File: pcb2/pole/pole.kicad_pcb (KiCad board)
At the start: 2 copper layers, 17 x 49 mm, 23 parts, among them IC1 LMx93, IC2 STM32F0xxKxUx, P1 POWER_IN, P2 BUS_IN, P3 BUS_OUT, P4 SWD_TC, P5 LEDs, Q1 MTM232270LBF, Q2 MTM232270LBF, Q3 MTM232270LBF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

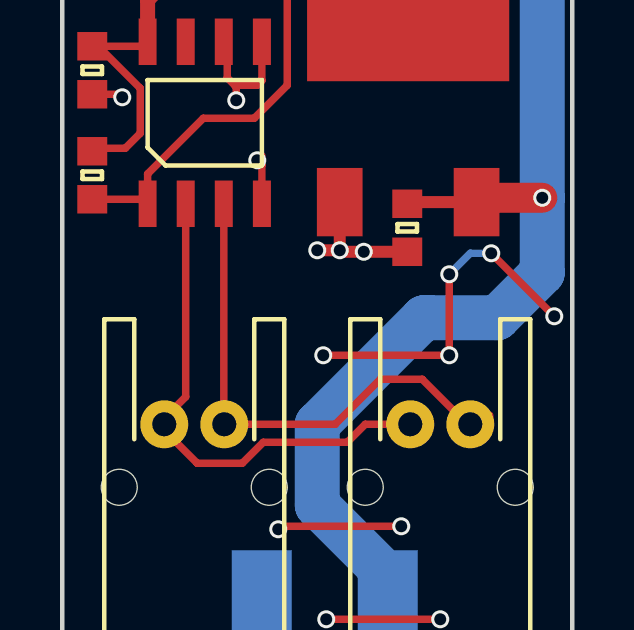
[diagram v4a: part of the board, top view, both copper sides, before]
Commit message: Added comparator receiver hysteresis
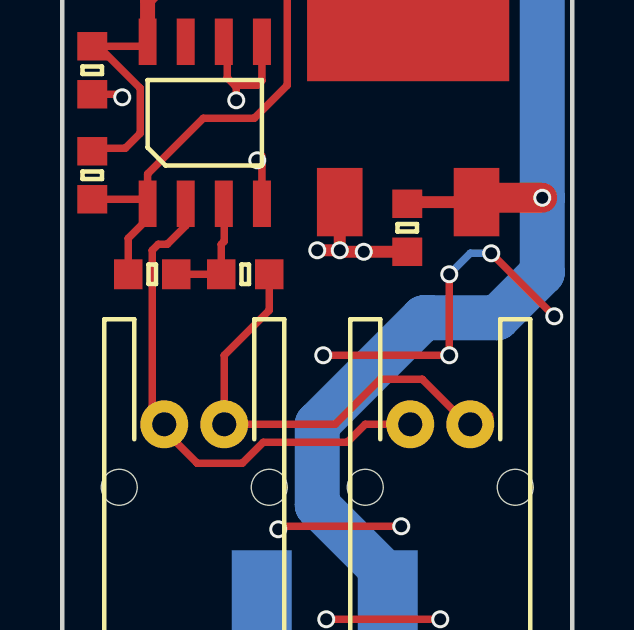
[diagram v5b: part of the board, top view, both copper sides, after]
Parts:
- added R2: 10k, agg:0603, F.Cu at (122.1, 101.3)
- added R3: 1M, agg:0603, F.Cu at (119.0, 101.3)
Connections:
- IC1 pad 3: /BUS_B -> Net-(IC1-Pad3)
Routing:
- net Net-(IC1-Pad3): track 0.00 -> 3.99 mm
- net /BUS: track 26.3 -> 29.0 mm
- net /BUS_B: track 17.5 -> 15.7 mm
- net /BUS_A: track 17.1 -> 17.8 mm
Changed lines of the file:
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@@
 (kicad_pcb (version 4) (host pcbnew 4.0.2-4+6225~38~ubuntu15.10.1-stable)
   (general
-    (links 59)
+    (links 62)
     (no_connects 0)
-    (area 114.894048 65.810714 134.355 127.725001)
+    (area 115.924999 65.924999 133.075001 115.075001)
     (thickness 1.6)
     (drawings 4)
-    (tracks 243)
+    (tracks 260)
     (zones 0)
-    (modules 23)
-    (nets 18)
+    (modules 25)
+    (nets 19)
   )
   (page A4)
@@
   (net 16 /LED_B)
   (net 17 "Net-(IC2-Pad4)")
+  (net 18 "Net-(IC1-Pad3)")
   (net_class Default "This is the default net class."
     (clearance 0.15)
@@
     (add_net /SWDIO)
     (add_net GND)
+    (add_net "Net-(IC1-Pad3)")
     (add_net "Net-(IC2-Pad4)")
     (add_net "Net-(Q4-Pad3)")
@@
       (net 5 /BUS_A))
     (pad 3 smd rect (at -2.7 0.635 90) (size 1.55 0.6) (layers F.Cu F.Paste F.Mask)
-      (net 6 /BUS_B))
+      (net 18 "Net-(IC1-Pad3)"))
     (pad 4 smd rect (at -2.7 1.905 90) (size 1.55 0.6) (layers F.Cu F.Paste F.Mask)
       (net 1 GND))
@@
     (pad 1 smd circle (at 0 0) (size 1 1) (layers F.Cu F.Mask)
       (net 17 "Net-(IC2-Pad4)"))
+  )
+  (module agg:0603 (layer F.Cu)
+    (at 122.1 101.3)
+    (fp_text reference R2 (at -2.225 0 90) (layer F.Fab) hide
+      (effects (font (size 1 1) (thickness 0.15)))
+    )
+    (fp_text value 10k (at 2.225 0 90) (layer F.Fab) hide
+      (effects (font (size 1 1) (thickness 0.15)))
+    )
+    (fp_line (start -0.8 -0.4) (end 0.8 -0.4) (layer F.Fab) (width 0.01))
+    (fp_line (start 0.8 -0.4) (end 0.8 0.4) (layer F.Fab) (width 0.01))
+    (fp_line (start 0.8 0.4) (end -0.8 0.4) (layer F.Fab) (width 0.01))
+    (fp_line (start -0.8 0.4) (end -0.8 -0.4) (layer F.Fab) (width 0.01))
+    (fp_line (start -0.45 -0.4) (end -0.45 0.4) (layer F.Fab) (width 0.01))
+    (fp_line (start 0.45 -0.4) (end 0.45 0.4) (layer F.Fab) (width 0.01))
+    (fp_line (start -0.125 -0.325) (end 0.125 -0.325) (layer F.SilkS) (width 0.15))
+    (fp_line (start 0.125 -0.325) (end 0.125 0.325) (layer F.SilkS) (width 0.15))
+    (fp_line (start 0.125 0.325) (end -0.125 0.325) (layer F.SilkS) (width 0.15))
+    (fp_line (start -0.125 0.325) (end -0.125 -0.325) (layer F.SilkS) (width 0.15))
+    (fp_line (start -1.55 -0.75) (end 1.55 -0.75) (layer F.CrtYd) (width 0.01))
+    (fp_line (start 1.55 -0.75) (end 1.55 0.75) (layer F.CrtYd) (width 0.01))
+    (fp_line (start 1.55 0.75) (end -1.55 0.75) (layer F.CrtYd) (width 0.01))
+    (fp_line (start -1.55 0.75) (end -1.55 -0.75) (layer F.CrtYd) (width 0.01))
+    (pad 1 smd rect (at -0.8 0) (size 0.95 1) (layers F.Cu F.Paste F.Mask)
+      (net 18 "Net-(IC1-Pad3)"))
+    (pad 2 smd rect (at 0.8 0) (size 0.95 1) (layers F.Cu F.Paste F.Mask)
+      (net 6 /BUS_B))
+  )
+  (module agg:0603 (layer F.Cu)
+    (at 119 101.3)
+    (fp_text reference R3 (at -2.225 0 90) (layer F.Fab) hide
+      (effects (font (size 1 1) (thickness 0.15)))
+    )
+    (fp_text value 1M (at 2.225 0 90) (layer F.Fab) hide
+      (effects (font (size 1 1) (thickness 0.15)))
+    )
+    (fp_line (start -0.8 -0.4) (end 0.8 -0.4) (layer F.Fab) (width 0.01))
+    (fp_line (start 0.8 -0.4) (end 0.8 0.4) (layer F.Fab) (width 0.01))
+    (fp_line (start 0.8 0.4) (end -0.8 0.4) (layer F.Fab) (width 0.01))
+    (fp_line (start -0.8 0.4) (end -0.8 -0.4) (layer F.Fab) (width 0.01))
+    (fp_line (start -0.45 -0.4) (end -0.45 0.4) (layer F.Fab) (width 0.01))
+    (fp_line (start 0.45 -0.4) (end 0.45 0.4) (layer F.Fab) (width 0.01))
+    (fp_line (start -0.125 -0.325) (end 0.125 -0.325) (layer F.SilkS) (width 0.15))
+    (fp_line (start 0.125 -0.325) (end 0.125 0.325) (layer F.SilkS) (width 0.15))
+    (fp_line (start 0.125 0.325) (end -0.125 0.325) (layer F.SilkS) (width 0.15))
+    (fp_line (start -0.125 0.325) (end -0.125 -0.325) (layer F.SilkS) (width 0.15))
+    (fp_line (start -1.55 -0.75) (end 1.55 -0.75) (layer F.CrtYd) (width 0.01))
+    (fp_line (start 1.55 -0.75) (end 1.55 0.75) (layer F.CrtYd) (width 0.01))
+    (fp_line (start 1.55 0.75) (end -1.55 0.75) (layer F.CrtYd) (width 0.01))
+    (fp_line (start -1.55 0.75) (end -1.55 -0.75) (layer F.CrtYd) (width 0.01))
+    (pad 1 smd rect (at -0.8 0) (size 0.95 1) (layers F.Cu F.Paste F.Mask)
+      (net 4 /BUS))
+    (pad 2 smd rect (at 0.8 0) (size 0.95 1) (layers F.Cu F.Paste F.Mask)
+      (net 18 "Net-(IC1-Pad3)"))
   )
   (gr_line (start 133 115) (end 116 115) (angle 90) (layer Edge.Cuts) (width 0.15))
@@
   (segment (start 130.25 68) (end 128.33 68) (width 1.5) (layer B.Cu) (net 3))
   (segment (start 130.475 98.95) (end 130.53 98.895) (width 0.25) (layer F.Cu) (net 3))
+  (segment (start 118.2 101.3) (end 118.2 100.1) (width 0.25) (layer F.Cu) (net 4))
+  (segment (start 118.2 100.1) (end 118.9 99.4) (width 0.25) (layer F.Cu) (net 4))
+  (segment (start 118.9 99.4) (end 118.9 99) (width 0.25) (layer F.Cu) (net 4))
+  (segment (start 118.9 99) (end 118.845 98.95) (width 0.25) (layer F.Cu) (net 4))
   (segment (start 118.845 98.95) (end 118.845 97.955) (width 0.25) (layer F.Cu) (net 4))
   (segment (start 120.5 83.2) (end 120.5 82.1) (width 0.25) (layer F.Cu) (net 4))
@@
   (segment (start 118.695 98.8) (end 118.845 98.95) (width 0.25) (layer F.Cu) (net 4))
   (segment (start 116.85 98.95) (end 116.75 99.05) (width 0.25) (layer F.Cu) (net 4))
+  (segment (start 120.115 98.95) (end 120.115 99.685) (width 0.25) (layer F.Cu) (net 5))
+  (segment (start 120.115 99.685) (end 119.5 100.3) (width 0.25) (layer F.Cu) (net 5))
+  (segment (start 119.5 100.3) (end 119.2 100.3) (width 0.25) (layer F.Cu) (net 5))
+  (segment (start 119.2 100.3) (end 119 100.5) (width 0.25) (layer F.Cu) (net 5))
+  (segment (start 119 100.5) (end 119 105.7) (width 0.25) (layer F.Cu) (net 5))
+  (segment (start 119 105.7) (end 119.4 106.1) (width 0.25) (layer F.Cu) (net 5))
+  (segment (start 119.4 106.1) (end 119.4 106.3) (width 0.25) (layer F.Cu) (net 5))
   (segment (start 127.6 106.3) (end 126.1 106.3) (width 0.25) (layer F.Cu) (net 5))
   (segment (start 120.5 107.6) (end 119.4 106.5) (width 0.25) (layer F.Cu) (net 5))
@@
   (segment (start 119.4 106.5) (end 119.4 106.3) (width 0.25) (layer F.Cu) (net 5))
   (segment (start 127.7 106.3) (end 127.6 106.3) (width 0.25) (layer F.Cu) (net 5))
-  (segment (start 120.115 98.95) (end 120.115 105.385) (width 0.25) (layer F.Cu) (net 5))
-  (segment (start 120.115 105.385) (end 119.4 106.1) (width 0.25) (layer F.Cu) (net 5))
   (segment (start 119.4 106.1) (end 119.4 106.3) (width 0.25) (layer F.Cu) (net 5))
+  (segment (start 121.4 106.3) (end 121.4 104) (width 0.25) (layer F.Cu) (net 6))
+  (segment (start 122.9 102.5) (end 122.9 101.3) (width 0.25) (layer F.Cu) (net 6))
+  (segment (start 121.4 104) (end 122.9 102.5) (width 0.25) (layer F.Cu) (net 6))
   (segment (start 121.4 106.3) (end 125.1 106.3) (width 0.25) (layer F.Cu) (net 6))
   (segment (start 128 104.8) (end 129.5 106.3) (width 0.25) (layer F.Cu) (net 6))
@@
   (segment (start 125.1 106.3) (end 126.6 104.8) (width 0.25) (layer F.Cu) (net 6))
   (segment (start 129.5 106.3) (end 129.6 106.3) (width 0.25) (layer F.Cu) (net 6))
-  (segment (start 121.385 98.95) (end 121.385 106.415) (width 0.25) (layer F.Cu) (net 6))
   (segment (start 121.385 106.415) (end 121.3 106.5) (width 0.25) (layer F.Cu) (net 6))
   (segment (start 121.3 106.5) (end 121.4 106.3) (width 0.25) (layer F.Cu) (net 6))
@@
   (segment (start 119.9 79.5) (end 119 79.5) (width 0.25) (layer F.Cu) (net 17))
   (segment (start 119 79.5) (end 118.6 79.1) (width 0.25) (layer F.Cu) (net 17))
+  (segment (start 119.8 101.3) (end 121.1 101.3) (width 0.25) (layer F.Cu) (net 18))
+  (segment (start 121.1 101.3) (end 121.3 101.3) (width 0.25) (layer F.Cu) (net 18))
+  (segment (start 121.3 101.3) (end 121.3 100.3) (width 0.25) (layer F.Cu) (net 18))
+  (segment (start 121.4 100.2) (end 121.4 98.9) (width 0.25) (layer F.Cu) (net 18))
+  (segment (start 121.3 100.3) (end 121.4 100.2) (width 0.25) (layer F.Cu) (net 18))
+  (segment (start 121.4 98.9) (end 121.385 98.95) (width 0.25) (layer F.Cu) (net 18))
   (zone (net 1) (net_name GND) (layer B.Cu) (hatch edge 0.508)
     (connect_pads (clearance 0.25))

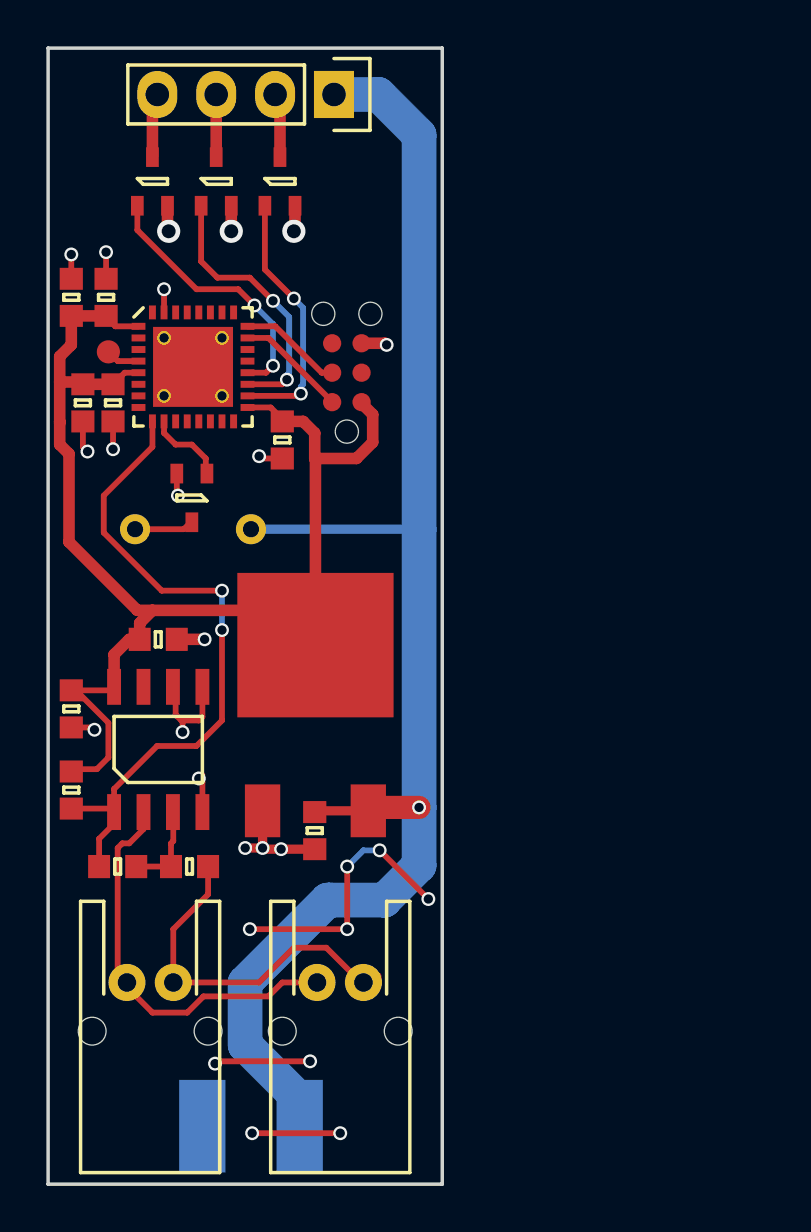
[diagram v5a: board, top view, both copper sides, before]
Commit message: re-layout and reroute of pole pcb
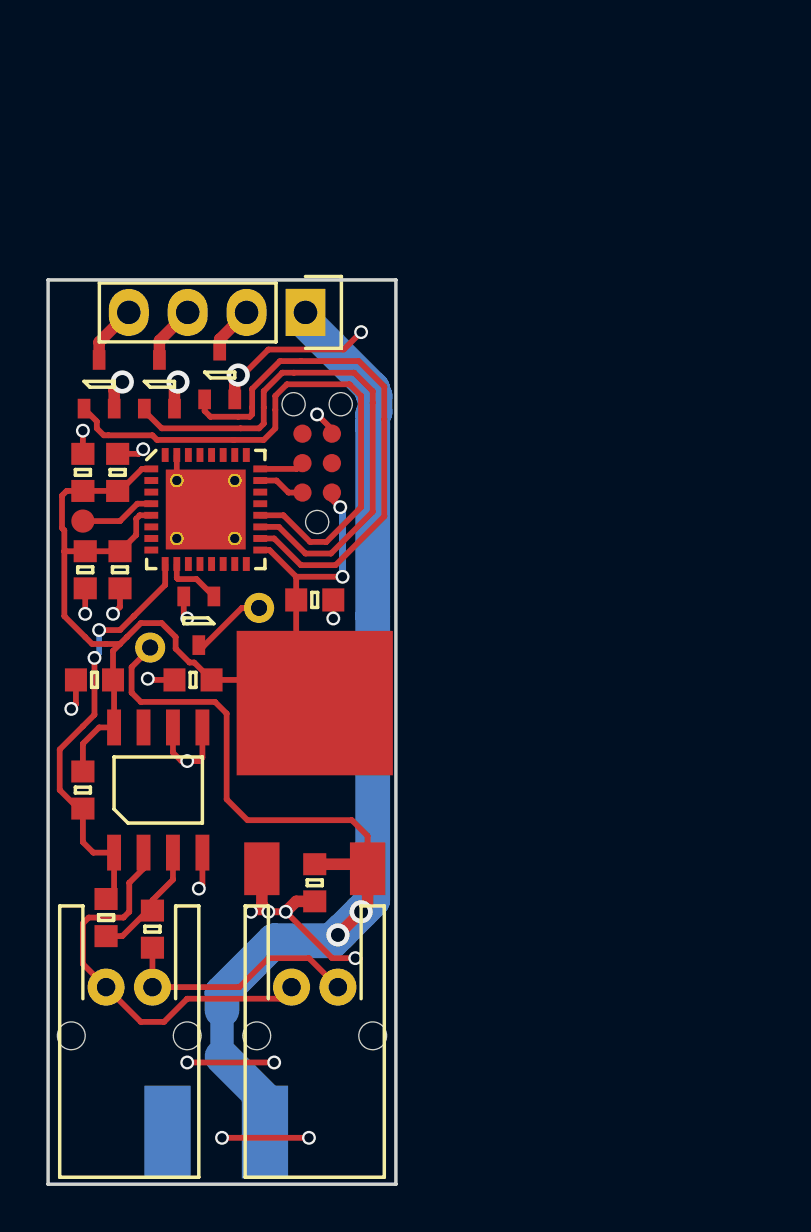
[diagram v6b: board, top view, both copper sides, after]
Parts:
- moved P5 9.48 mm to (127.1, 77.4)
- moved Q2 9.09 mm to (120.8, 80.5)
- moved Q3 9.05 mm to (118.2, 80.5)
- moved Q1 8.75 mm to (123.4, 80.1)
- moved C2 7.57 mm to (117.5, 84.3)
- moved C3 7.57 mm to (119.0, 84.3)
- moved TP1 7.38 mm to (117.5, 86.4)
- moved C4 7.21 mm to (119.1, 88.5)
- moved C8 7.20 mm to (117.6, 88.5)
- moved C5 7.04 mm to (127.5, 89.8), turned to 0 degrees
- moved IC2 6.17 mm to (122.8, 85.9)
- moved Q4 5.31 mm to (122.5, 90.7)
- moved SP1 4.28 mm to (122.8, 91.0), turned to 20 degrees
- moved P4 4.10 mm to (127.6, 83.9)
- moved R2 3.14 mm to (120.5, 104.0), turned to 270 degrees
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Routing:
- net /LED_B: track 11.6 -> 25.0 mm, vias 2 -> 0
- net (no net): track 19.5 -> 7.50 mm, vias 9 -> 4
- net /LED_G: track 11.7 -> 23.7 mm, vias 2 -> 0
- net /LED_R: track 11.2 -> 22.7 mm, vias 2 -> 0
- net /BUS: track 29.0 -> 18.6 mm
- net GND: track 27.0 -> 35.3 mm, vias 18 -> 19
- net /BUS_B: track 15.7 -> 10.7 mm
- net +12V: track 64.7 -> 67.6 mm, vias 1 -> 2
- net /SWDIO: track 4.81 -> 2.04 mm
- net +3V3: track 58.5 -> 55.8 mm, vias 0 -> 2
- net /SWDCLK: track 4.48 -> 1.92 mm
- net Net-(IC2-Pad4): track 1.47 -> 3.26 mm
- net Net-(IC1-Pad3): track 3.99 -> 5.32 mm
- net /PIEZO: track 3.41 -> 2.53 mm
- net Net-(Q4-Pad3): track 2.57 -> 3.28 mm
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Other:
- board size 17 x 49 mm -> 15 x 39 mm

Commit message: Added pole silk
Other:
- board text added: "2016-03-28"
- board text added: "DAVID TURNER ADAM GREIG"
- board text added: "Revision 1"
- board text added: "THE·GRID"
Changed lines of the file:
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@@
     (area 114.7 74.160714 133.125 127.975001)
     (thickness 1.6)
-    (drawings 4)
+    (drawings 8)
     (tracks 286)
     (zones 0)
@@
       (net 18 "Net-(IC1-Pad3)"))
   )
+  (gr_text "Revision 1" (at 121.75 81.75) (layer B.SilkS)
+    (effects (font (size 1 1) (thickness 0.15)) (justify mirror))
+  )
+  (gr_text 2016-03-28 (at 125.5 83.25) (layer B.SilkS)
+    (effects (font (size 1 1) (thickness 0.15)) (justify mirror))
+  )
+  (gr_text "DAVID TURNER\nADAM GREIG" (at 122.25 101.5) (layer B.SilkS)
+    (effects (font (size 1 1) (thickness 0.15)) (justify mirror))
+  )
+  (gr_text THE·GRID (at 122.25 98.75) (layer B.SilkS)
+    (effects (font (size 1.5 1.5) (thickness 0.3)) (justify mirror))
+  )
   (gr_line (start 131 115) (end 131 76) (angle 90) (layer Edge.Cuts) (width 0.15))
